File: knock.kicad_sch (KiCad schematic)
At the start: 28 parts, among them J7 AudioJack3, U7 MCP6004, U8 MCP6002-xSN

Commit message: USB jack, parts and LCSC numbers, headphone jack
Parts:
- J7: footprint Connector_Audio:Jack_3.5mm_CUI_SJ1-3533NG_Horizontal -> audiojack:Jack_3.5mm_PJ-3250-5A; LCSC N/A -> C165947
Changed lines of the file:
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@@
       (effects (font (size 1.27 1.27)) (justify right))
     )
-    (property "Footprint" "Connector_Audio:Jack_3.5mm_CUI_SJ1-3533NG_Horizontal" (at 258.445 46.355 0)
+    (property "Footprint" "audiojack:Jack_3.5mm_PJ-3250-5A" (at 258.445 46.355 0)
       (effects (font (size 1.27 1.27)) hide)
     )
@@
       (effects (font (size 1.27 1.27)) hide)
     )
-    (property "LCSC" "N/A" (at 258.445 46.355 0)
+    (property "LCSC" "C165947" (at 258.445 46.355 0)
       (effects (font (size 1.27 1.27)) hide)
     )

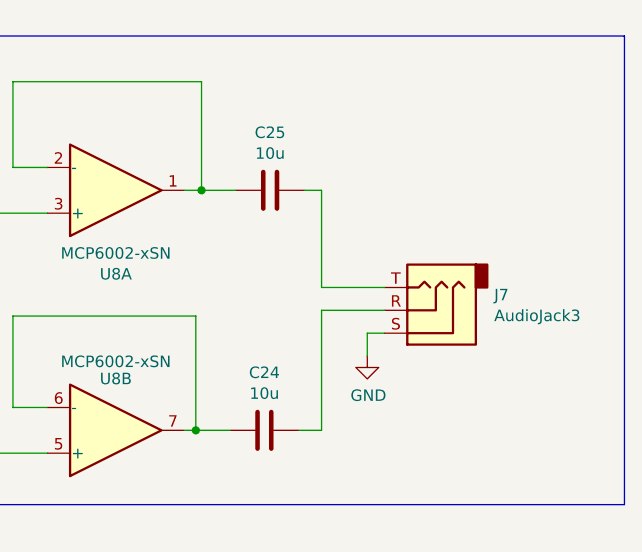
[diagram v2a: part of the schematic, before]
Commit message: Fix connector, optimize psu
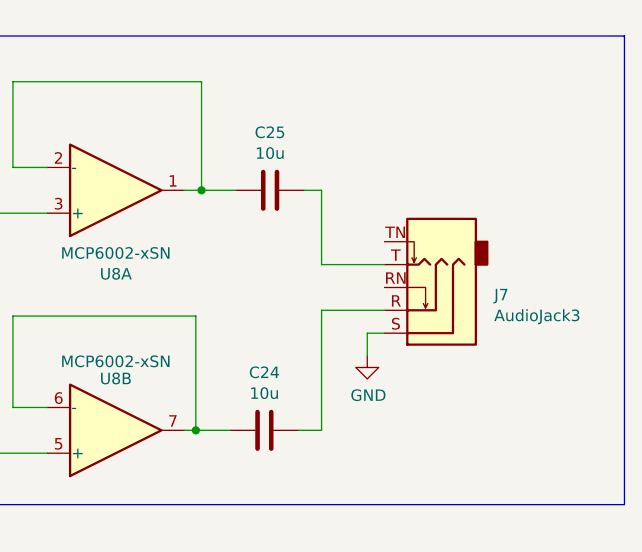
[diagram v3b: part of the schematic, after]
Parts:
- J7: symbol Connector:AudioJack3 -> Connector_Audio:AudioJack3_SwitchTR
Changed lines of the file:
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@@
     (stroke (width 0) (type default))
   )
-  (wire (pts (xy 246.38 33.02) (xy 246.38 43.815))
+  (wire (pts (xy 246.38 33.02) (xy 246.38 41.275))
     (stroke (width 0) (type default))
   )
@@
     (stroke (width 0) (type default))
   )
-  (wire (pts (xy 246.38 43.815) (xy 253.365 43.815))
+  (wire (pts (xy 246.38 41.275) (xy 253.365 41.275))
     (stroke (width 0) (type default))
   )
@@
     )
   )
-  (symbol (lib_id "Connector:AudioJack3") (at 258.445 46.355 180) (unit 1)
+  (symbol (lib_id "Connector_Audio:AudioJack3_SwitchTR") (at 258.445 46.355 180) (unit 1)
     (in_bom yes) (on_board yes) (dnp no)
     (property "Reference" "J7" (at 265.557 44.6532 0)
@@
     )
     (pin "R")
+    (pin "RN")
     (pin "S")
     (pin "T")
-    (instances
-      (project "proteus"
+    (pin "TN")
+    (instances
+      (project "proteus"

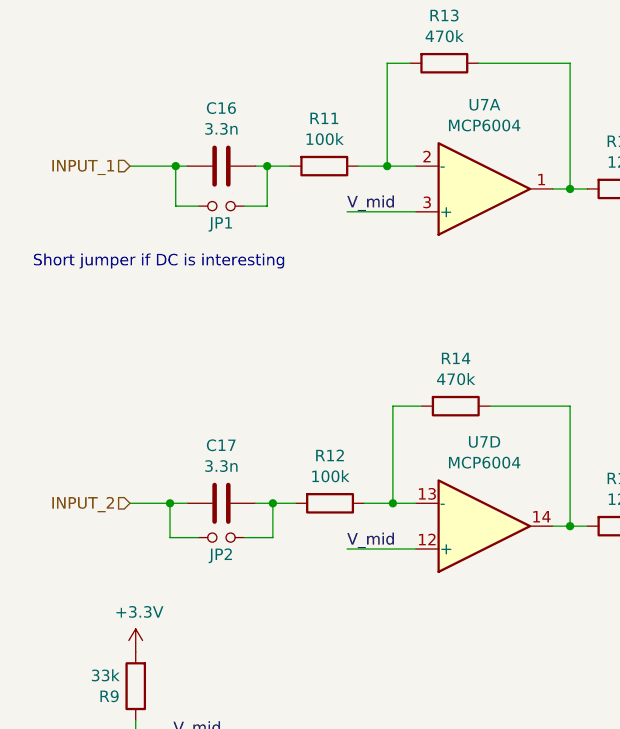
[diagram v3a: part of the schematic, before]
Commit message: Add Stepper, fix Connector, add Testpoints, several changes
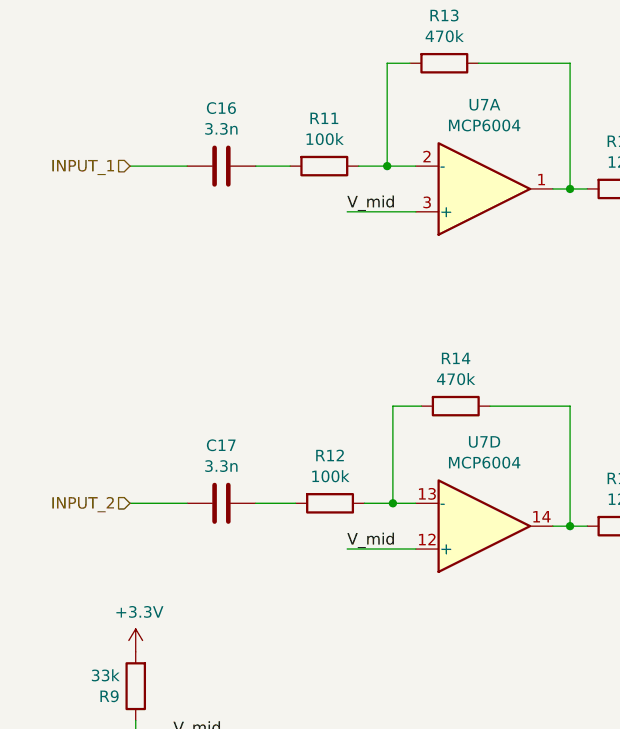
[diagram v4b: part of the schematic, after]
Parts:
- removed JP1, JP2: Jumper_NO_Small, Jumper:SolderJumper-2_P1.3mm_Open_TrianglePad1.0x1.5mm, symbol proteus-rescue:Jumper_NO_Small-Device
- C16, C17: LCSC C53175 -> C107149
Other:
- note removed: "Short jumper if DC is interesting"
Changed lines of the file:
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@@
     (comment 2 "rusefi.com/s/proteus")
   )
-  (junction (at 52.705 69.85) (diameter 0) (color 0 0 0 0)
-  )
   (junction (at 108.585 72.39) (diameter 0) (color 0 0 0 0)
   )
@@
   (junction (at 120.015 34.925) (diameter 0) (color 0 0 0 0)
   )
-  (junction (at 52.07 32.385) (diameter 0) (color 0 0 0 0)
-  )
   (junction (at 108.585 34.925) (diameter 0) (color 0 0 0 0)
   )
-  (junction (at 41.275 69.85) (diameter 0) (color 0 0 0 0)
-  )
   (junction (at 85.725 72.39) (diameter 0) (color 0 0 0 0)
   )
@@
   (junction (at 233.045 33.02) (diameter 0) (color 0 0 0 0)
   )
-  (junction (at 41.91 32.385) (diameter 0) (color 0 0 0 0)
-  )
   (junction (at 139.065 32.385) (diameter 0) (color 0 0 0 0)
   )
   (junction (at 139.065 69.85) (diameter 0) (color 0 0 0 0)
   )
-  (wire (pts (xy 50.8 69.85) (xy 52.705 69.85))
+  (wire (pts (xy 50.8 69.85) (xy 55.245 69.85))
     (stroke (width 0) (type default))
   )
@@
     (stroke (width 0) (type default))
   )
-  (wire (pts (xy 41.275 73.66) (xy 41.275 69.85))
-    (stroke (width 0) (type default))
-  )
   (wire (pts (xy 108.585 21.59) (xy 108.585 34.925))
     (stroke (width 0) (type default))
@@
     (stroke (width 0) (type default))
   )
-  (wire (pts (xy 41.91 32.385) (xy 43.18 32.385))
-    (stroke (width 0) (type default))
-  )
   (wire (pts (xy 212.09 30.48) (xy 212.09 20.955))
     (stroke (width 0) (type default))
@@
     (stroke (width 0) (type default))
   )
-  (wire (pts (xy 36.83 69.85) (xy 41.275 69.85))
-    (stroke (width 0) (type default))
-  )
-  (wire (pts (xy 50.8 32.385) (xy 52.07 32.385))
+  (wire (pts (xy 36.83 69.85) (xy 43.18 69.85))
+    (stroke (width 0) (type default))
+  )
+  (wire (pts (xy 50.8 32.385) (xy 54.61 32.385))
     (stroke (width 0) (type default))
   )
@@
     (stroke (width 0) (type default))
   )
-  (wire (pts (xy 36.83 32.385) (xy 41.91 32.385))
+  (wire (pts (xy 36.83 32.385) (xy 43.18 32.385))
     (stroke (width 0) (type default))
   )
@@
     (stroke (width 0) (type default))
   )
-  (wire (pts (xy 41.91 36.83) (xy 41.91 32.385))
-    (stroke (width 0) (type default))
-  )
   (polyline (pts (xy 280.035 15.875) (xy 280.035 67.945))
     (stroke (width 0) (type default))
@@
     (stroke (width 0) (type default))
   )
-  (wire (pts (xy 52.07 36.83) (xy 52.07 32.385))
-    (stroke (width 0) (type default))
-  )
   (wire (pts (xy 37.465 93.98) (xy 37.465 95.885))
     (stroke (width 0) (type default))
@@
     (stroke (width 0) (type default))
   )
-  (wire (pts (xy 44.45 36.83) (xy 41.91 36.83))
-    (stroke (width 0) (type default))
-  )
   (wire (pts (xy 231.14 33.02) (xy 233.045 33.02))
     (stroke (width 0) (type default))
@@
     (stroke (width 0) (type default))
   )
-  (wire (pts (xy 52.705 69.85) (xy 55.245 69.85))
-    (stroke (width 0) (type default))
-  )
   (wire (pts (xy 62.865 69.85) (xy 66.04 69.85))
     (stroke (width 0) (type default))
@@
     (stroke (width 0) (type default))
   )
-  (wire (pts (xy 49.53 36.83) (xy 52.07 36.83))
-    (stroke (width 0) (type default))
-  )
   (wire (pts (xy 253.365 46.355) (xy 246.38 46.355))
     (stroke (width 0) (type default))
@@
     (stroke (width 0) (type default))
   )
-  (wire (pts (xy 52.07 32.385) (xy 54.61 32.385))
-    (stroke (width 0) (type default))
-  )
   (wire (pts (xy 120.015 72.39) (xy 118.11 72.39))
     (stroke (width 0) (type default))
   )
-  (wire (pts (xy 52.705 73.66) (xy 52.705 69.85))
-    (stroke (width 0) (type default))
-  )
   (wire (pts (xy 139.065 32.385) (xy 137.16 32.385))
     (stroke (width 0) (type default))
@@
     (stroke (width 0) (type default))
   )
-  (wire (pts (xy 49.53 73.66) (xy 52.705 73.66))
-    (stroke (width 0) (type default))
-  )
   (wire (pts (xy 66.04 69.85) (xy 66.04 59.055))
     (stroke (width 0) (type default))
@@
     (stroke (width 0) (type default))
   )
-  (wire (pts (xy 41.275 69.85) (xy 43.18 69.85))
-    (stroke (width 0) (type default))
-  )
   (wire (pts (xy 231.14 59.69) (xy 232.41 59.69))
     (stroke (width 0) (type default))
@@
     (stroke (width 0) (type default))
   )
-  (wire (pts (xy 44.45 73.66) (xy 41.275 73.66))
-    (stroke (width 0) (type default))
-  )
   (wire (pts (xy 110.49 21.59) (xy 108.585 21.59))
     (stroke (width 0) (type default))
@@
   )
   (text "Line Out" (at 186.055 20.32 0)
-    (effects (font (size 1.27 1.27)) (justify left bottom))
-  )
-  (text "Short jumper if DC is interesting" (at 26.035 43.815 0)
     (effects (font (size 1.27 1.27)) (justify left bottom))
   )
@@
       (effects (font (size 1.27 1.27)) hide)
     )
-    (property "LCSC" "C53175" (at 46.99 32.385 0)
+    (property "LCSC" "C107149" (at 46.99 32.385 0)
       (effects (font (size 1.27 1.27)) hide)
     )
@@
       (effects (font (size 1.27 1.27)) hide)
     )
-    (property "LCSC" "C53175" (at 46.99 69.85 0)
+    (property "LCSC" "C107149" (at 46.99 69.85 0)
       (effects (font (size 1.27 1.27)) hide)
     )
@@
         )
       )
-    )
-  )
-  (symbol (lib_id "proteus-rescue:Jumper_NO_Small-Device") (at 46.99 36.83 0) (unit 1)
-    (in_bom yes) (on_board yes) (dnp no)
-    (property "Reference" "JP1" (at 46.99 38.735 0)
-      (effects (font (size 1.27 1.27)))
-    )
-    (property "Value" "Jumper_NO_Small" (at 46.99 48.895 0)
-      (effects (font (size 1.27 1.27)) hide)
-    )
-    (property "Footprint" "Jumper:SolderJumper-2_P1.3mm_Open_TrianglePad1.0x1.5mm" (at 46.99 36.83 0)
-      (effects (font (size 1.27 1.27)) hide)
-    )
-    (property "Datasheet" "~" (at 46.99 36.83 0)
-      (effects (font (size 1.27 1.27)) hide)
-    )
-    (property "LCSC" "N/A" (at 46.99 36.83 0)
-      (effects (font (size 1.27 1.27)) hide)
-    )
-    (pin "1")
-    (pin "2")
-    (instances
-      (project "proteus"
-        (path "/d9116601-cae2-4199-827b-70fa136aae51/00000000-0000-0000-0000-00005e814213"
-          (reference "JP1") (unit 1)
-        )
-      )
-    )
-  )
-  (symbol (lib_id "proteus-rescue:Jumper_NO_Small-Device") (at 46.99 73.66 0) (unit 1)
-    (in_bom yes) (on_board yes) (dnp no)
-    (property "Reference" "JP2" (at 46.99 75.565 0)
-      (effects (font (size 1.27 1.27)))
-    )
-    (property "Value" "Jumper_NO_Small" (at 46.99 85.725 0)
-      (effects (font (size 1.27 1.27)) hide)
-    )
-    (property "Footprint" "Jumper:SolderJumper-2_P1.3mm_Open_TrianglePad1.0x1.5mm" (at 46.99 73.66 0)
-      (effects (font (size 1.27 1.27)) hide)
-    )
-    (property "Datasheet" "~" (at 46.99 73.66 0)
-      (effects (font (size 1.27 1.27)) hide)
-    )
-    (property "LCSC" "N/A" (at 46.99 73.66 0)
-      (effects (font (size 1.27 1.27)) hide)
-    )
-    (pin "1")
-    (pin "2")
-    (instances
-      (project "proteus"
-        (path "/d9116601-cae2-4199-827b-70fa136aae51/00000000-0000-0000-0000-00005e814213"
-          (reference "JP2") (unit 1)
-        )
-      )

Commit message: Production optimizations, voltage superv, etb sv conn
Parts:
- J7: JLCPosOffset (none) -> 0.75,-2.25
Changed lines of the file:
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@@
+      (effects (font (size 1.27 1.27)) hide)
+    )
+    (property "JLCPosOffset" "0.75,-2.25" (at 258.445 46.355 0)
       (effects (font (size 1.27 1.27)) hide)
     )
